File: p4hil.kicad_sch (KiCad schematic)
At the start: 7 parts, among them J14 Conn_01x04, SW1 SW_Push, SW2 SW_Push

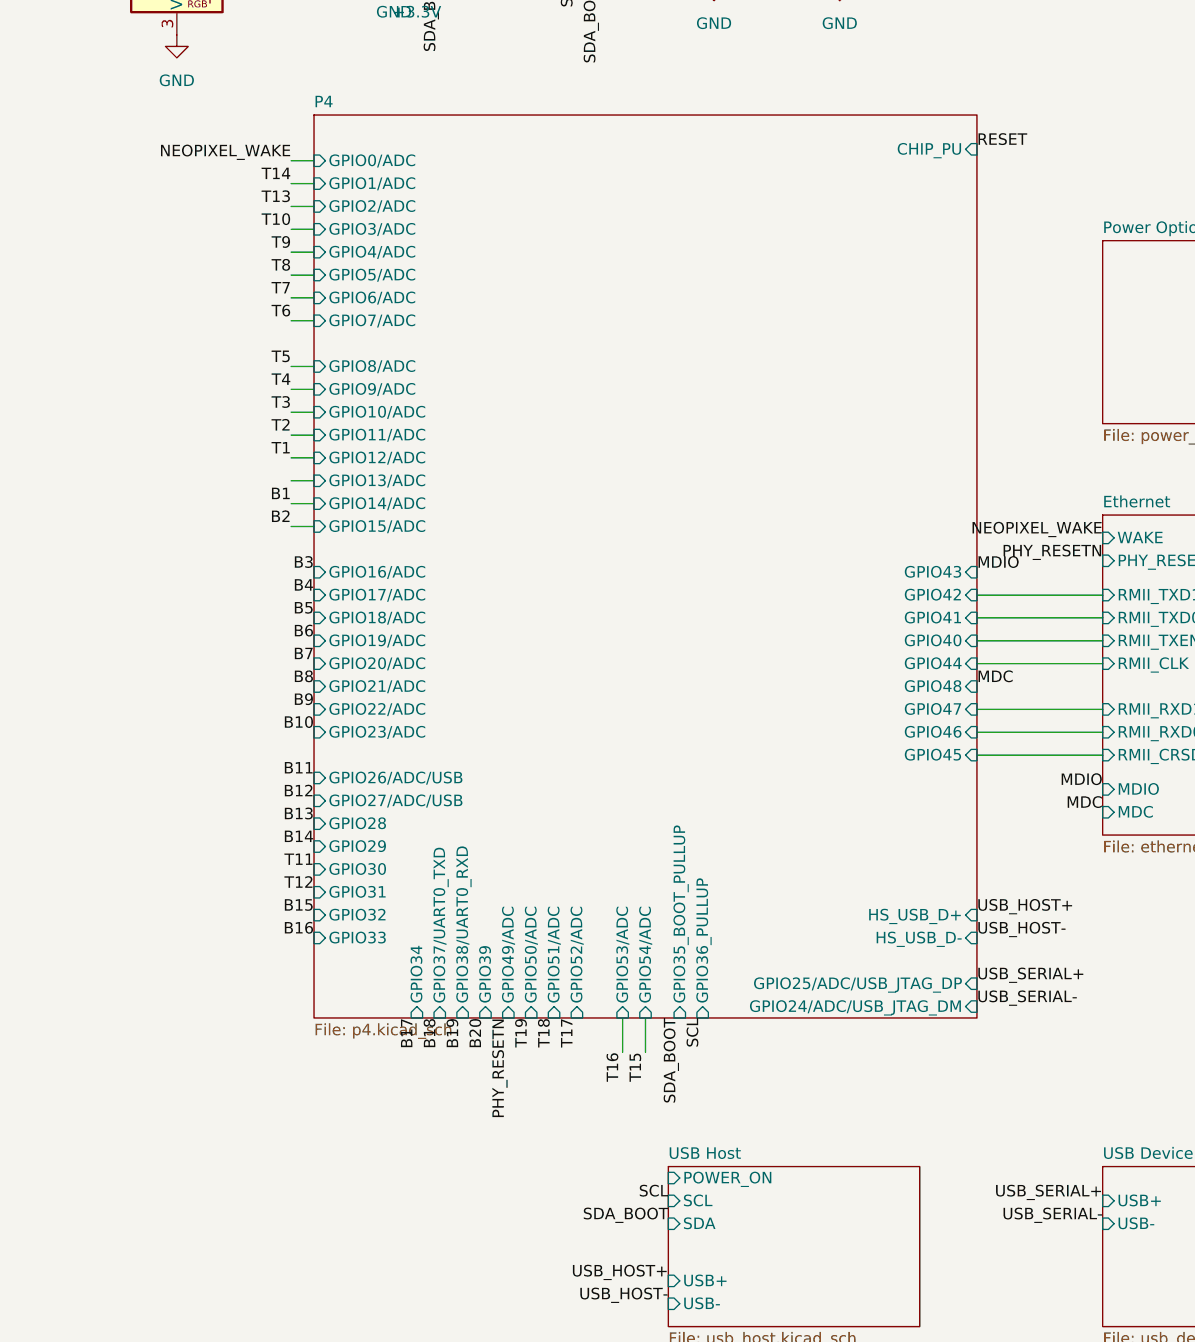
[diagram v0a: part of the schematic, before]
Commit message: Lots more routing
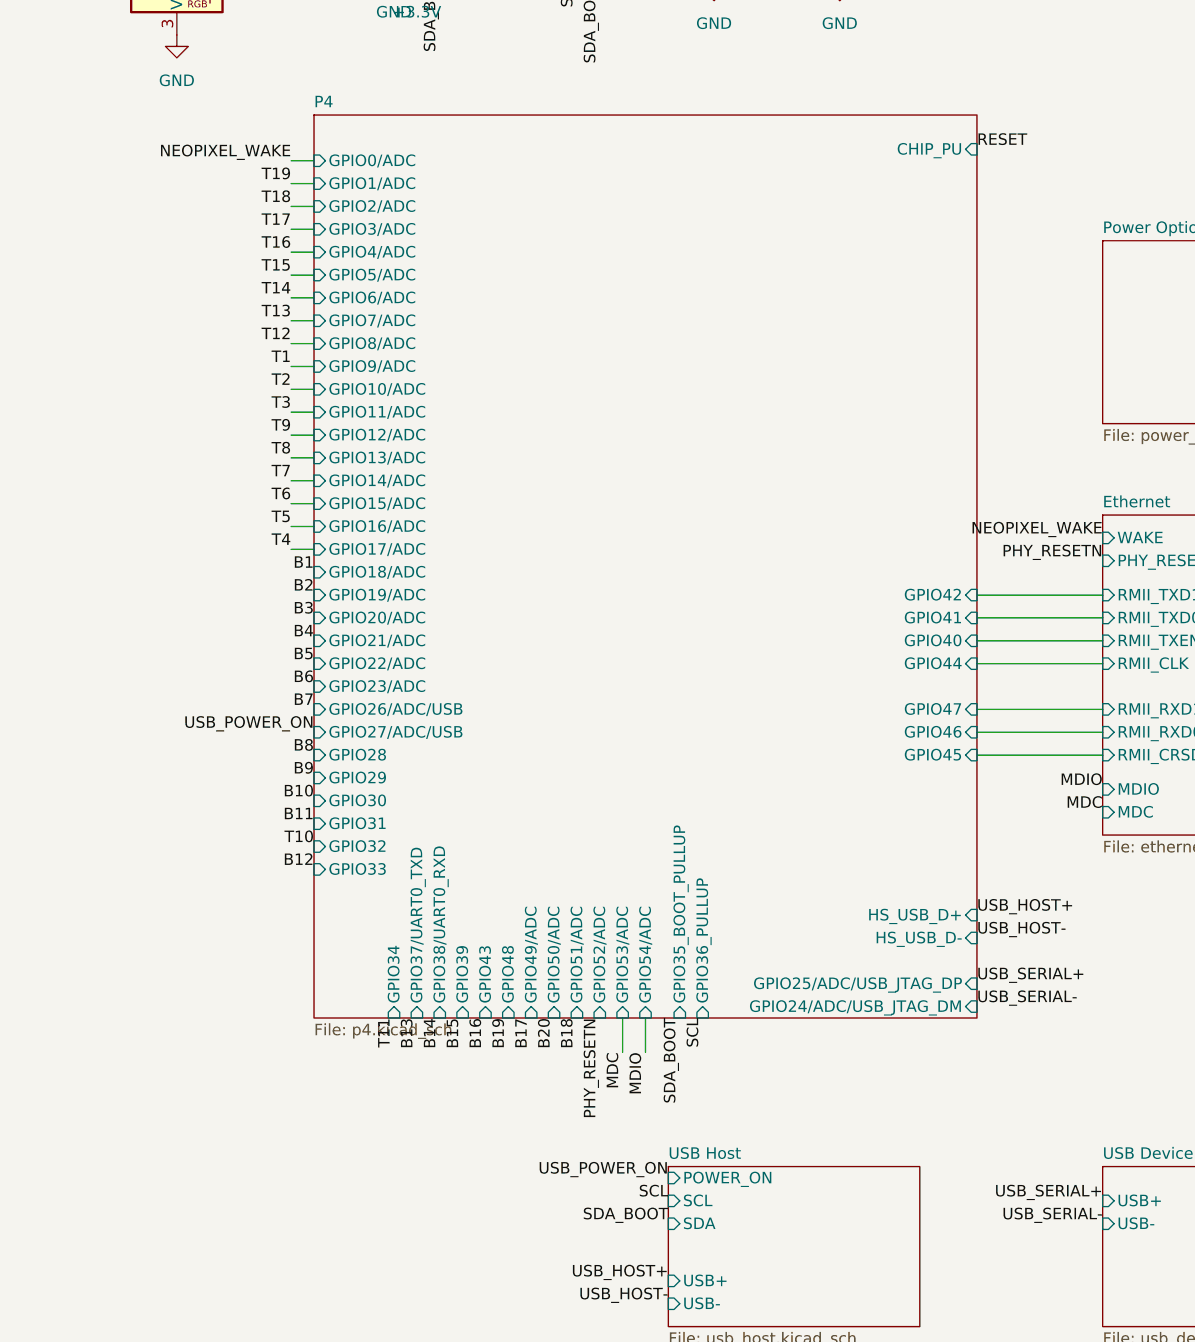
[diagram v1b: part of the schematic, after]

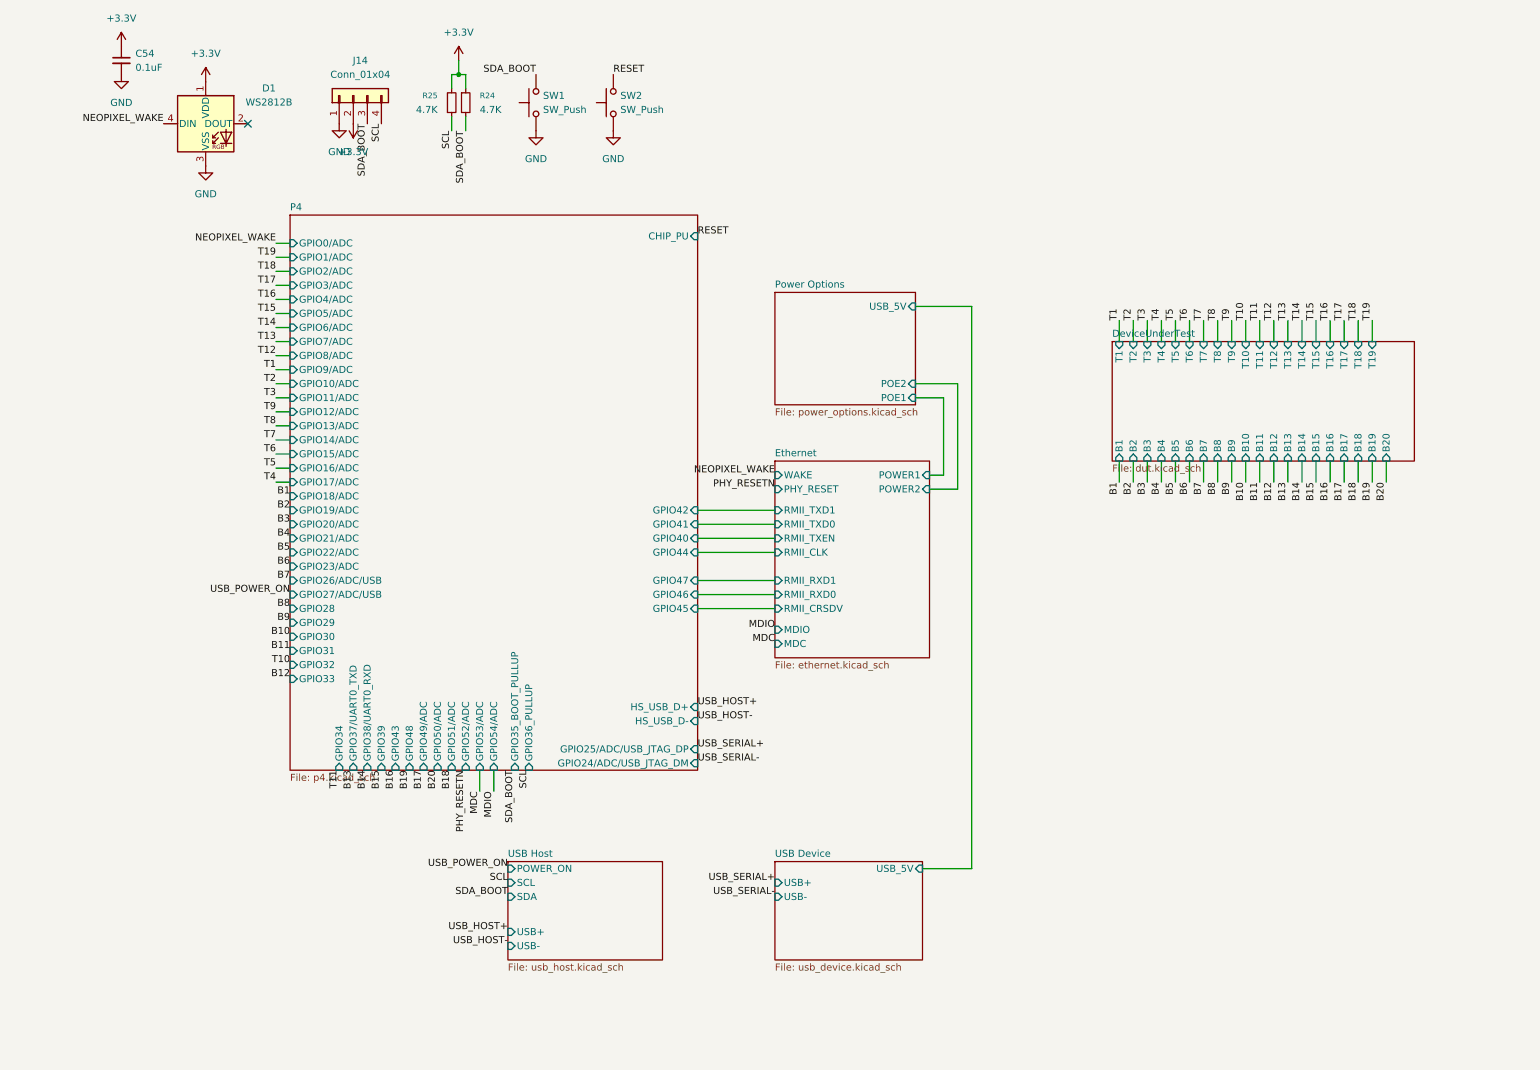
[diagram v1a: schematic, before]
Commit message: gah, need i2c expander for pull control
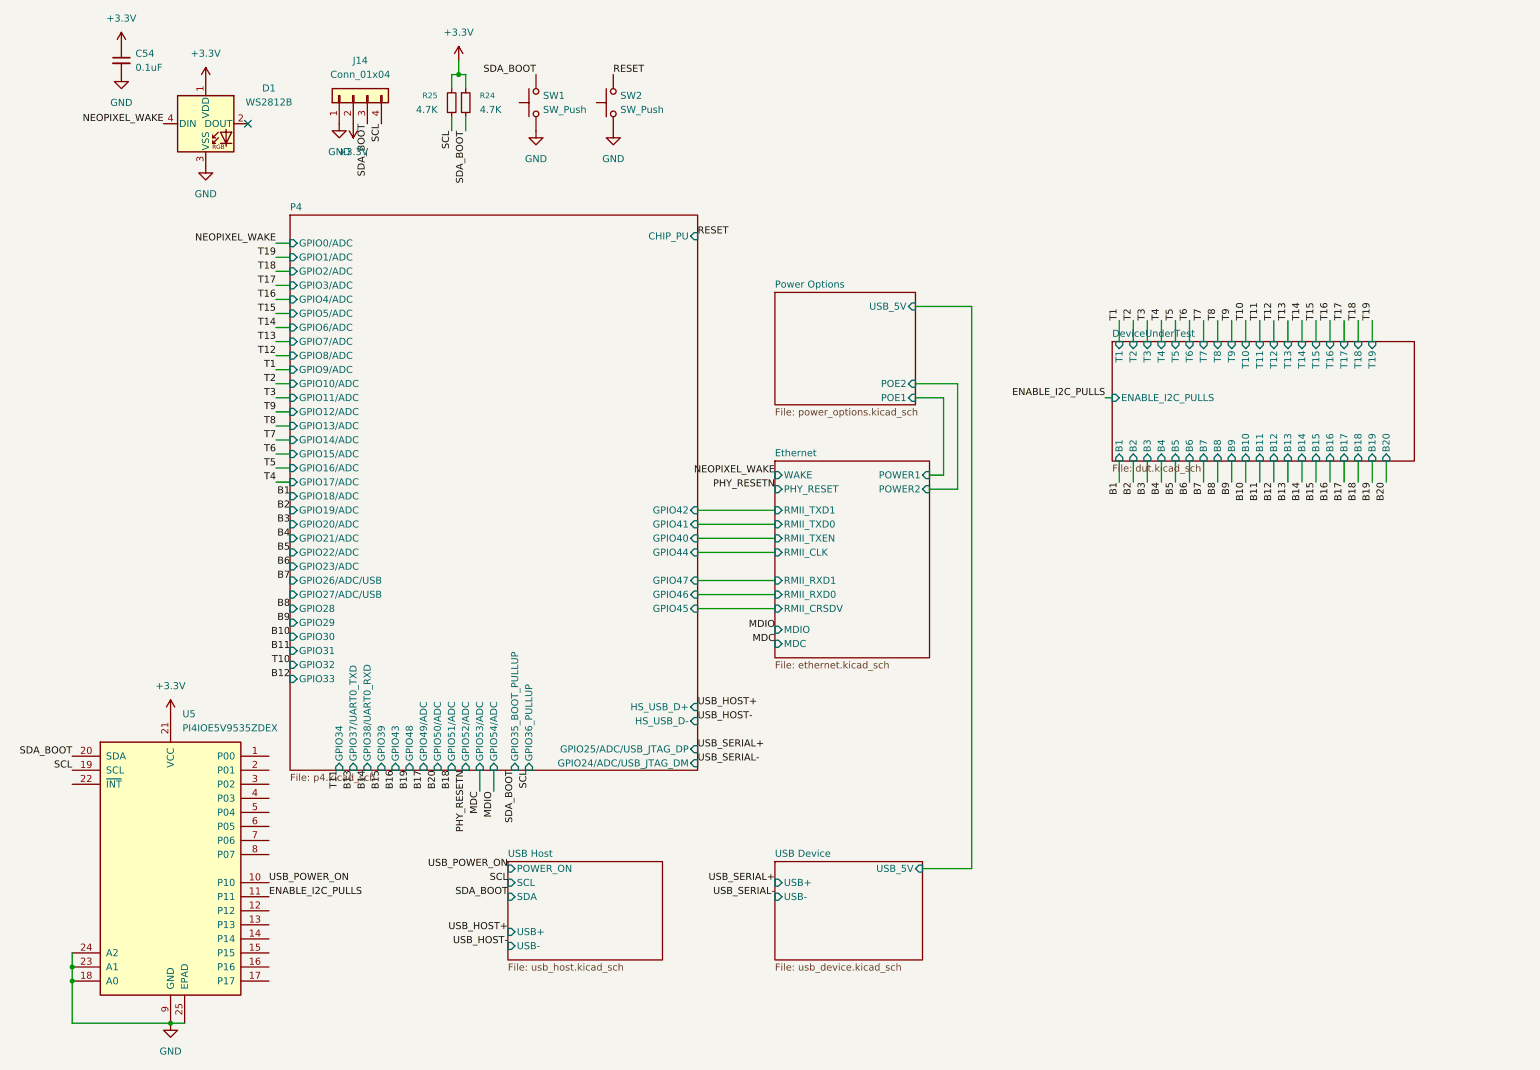
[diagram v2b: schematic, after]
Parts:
- added U5: PI4IOE5V9535ZDEX, Package_DFN_QFN:VQFN-24-1EP_4x4mm_P0.5mm_EP2.45x2.45mm, symbol Interface_Expansion:TCA9535RGER
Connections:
- net +3.3V: now also U5.21 (VCC)
- net GND: now also U5.18 (A0), U5.23 (A1), U5.24 (A2), U5.25 (EPAD), U5.9 (GND)
- net SCL: now also U5.19 (SCL)
- net SDA_BOOT: now also U5.20 (SDA)
- net USB_POWER_ON: now also U5.10 (P10)
- new net ENABLE_I2C_PULLS: U5.11 (P11)
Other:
- sheet DeviceUnderTest ports: added ENABLE_I2C_PULLS; removed none

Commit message: clean drc
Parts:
- added C60: 0.1uF, Capacitor_SMD:C_0402_1005Metric, symbol Device:C_Small
- added J20: Conn_02x04_Odd_Even, Connector_PinHeader_2.54mm:PinHeader_2x04_P2.54mm_Vertical, symbol Connector_Generic:Conn_02x04_Odd_Even
- added J21: Conn_01x06, Connector_PinHeader_2.54mm:PinHeader_1x06_P2.54mm_Vertical, symbol Connector_Generic:Conn_01x06
- added PORT5: LED_Small, LED_SMD:LED_0603_1608Metric, symbol Device:LED_Small
- added R73: 470, Resistor_SMD:R_0402_1005Metric, symbol Device:R_Small
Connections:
- net +3.3V: now also C60.1, PORT5.2 (A)
- net ENABLE_I2C_PULLS: now also U5.8 (P07); no longer U5.11 (P11)
- net GND: now also C60.2
- net USB_POWER_ON: no longer U5.10 (P10)
- net P00: now reaches U5.1 (P00)
- net P00: now also J21.1 (Pin_1)
- net P12: now reaches U5.12 (P12)
- net P12: now also J20.8 (Pin_8)
- net P13: now reaches U5.13 (P13)
- net P13: now also J20.6 (Pin_6)
- net P14: now reaches U5.14 (P14)
- net P14: now also J20.3 (Pin_3)
- net P15: now reaches U5.15 (P15)
- net P15: now also J20.4 (Pin_4)
- net P16: now reaches U5.16 (P16)
- net P16: now also J20.1 (Pin_1)
- net P17: now reaches U5.17 (P17)
- net P17: now also J20.2 (Pin_2)
- net P01: now reaches U5.2 (P01)
- net P01: now also J21.2 (Pin_2)
- net P02: now reaches U5.3 (P02)
- net P02: now also J21.3 (Pin_3)
- net P03: now reaches U5.4 (P03)
- net P03: now also J21.4 (Pin_4)
- net P04: now reaches U5.5 (P04)
- net P04: now also J21.5 (Pin_5)
- net P05: now reaches U5.6 (P05)
- net P05: now also J21.6 (Pin_6)
- net P06: now reaches U5.7 (P06)
- net P06: now also R73.2
- new net: PORT5.1 (K), R73.1
- new net P10: J20.7 (Pin_7), U5.10 (P10)
- new net P11: J20.5 (Pin_5), U5.11 (P11)
- no-connect marks 1 -> 2
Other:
- moved on the sheet: U5

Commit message: v1
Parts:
- R73: value 470 -> 4.7K
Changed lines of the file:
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@@
 			)
 		)
-		(property "Value" "470"
+		(property "Value" "4.7K"
 			(at 224.79 146.0499 0)
 			(show_name no)

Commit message: Start v2
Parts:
- removed C60: 0.1uF, Capacitor_SMD:C_0402_1005Metric, symbol Device:C_Small
- removed J20: Conn_02x04_Odd_Even, Connector_PinHeader_2.54mm:PinHeader_2x04_P2.54mm_Vertical, symbol Connector_Generic:Conn_02x04_Odd_Even
- removed J21: Conn_01x06, Connector_PinHeader_2.54mm:PinHeader_1x06_P2.54mm_Vertical, symbol Connector_Generic:Conn_01x06
- removed PORT5: LED_Small, LED_SMD:LED_0603_1608Metric, symbol Device:LED_Small
- removed R73: 4.7K, Resistor_SMD:R_0402_1005Metric, symbol Device:R_Small
- removed U5: PI4IOE5V9535ZDEX, Package_DFN_QFN:VQFN-24-1EP_4x4mm_P0.5mm_EP2.45x2.45mm, symbol Interface_Expansion:TCA9535RGER
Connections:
- no-connect marks 2 -> 1
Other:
- sheet DeviceUnderTest ports: added none; removed ENABLE_I2C_PULLS
- sheet Power Options ports: added none; removed POE1, POE2, USB_5V
